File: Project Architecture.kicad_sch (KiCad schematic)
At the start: 0 parts

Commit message: Final Changes, Updated to Checked
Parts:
- added H1, H2, H3, H4: MountingHole_Pad, MountingHole:MountingHole_3.2mm_M3_DIN965_Pad, symbol Mechanical:MountingHole_Pad
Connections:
- no-connect marks 0 -> 4
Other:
- added sheet Section D - RTC (rtc.kicad_sch)
- sheet Section A - Title A ports: added I2C_SCL, I2C_SDA; removed none
- note added: "Page 9"

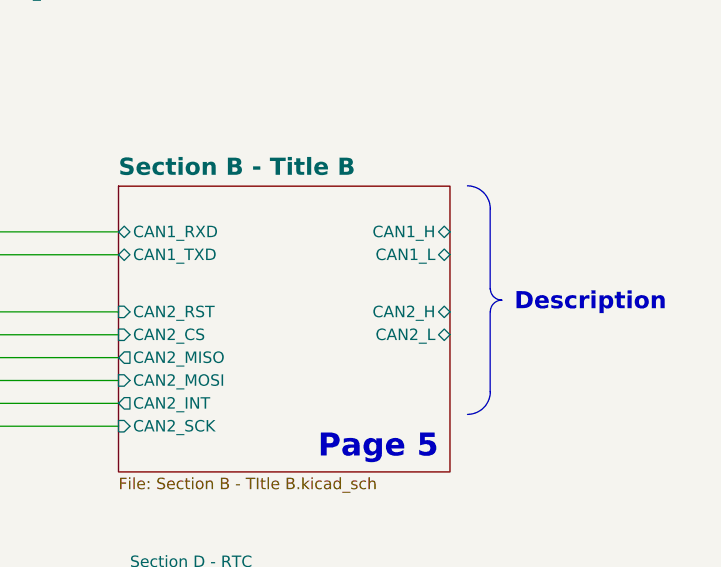
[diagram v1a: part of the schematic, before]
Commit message: Retry with rules DRC ERC passing
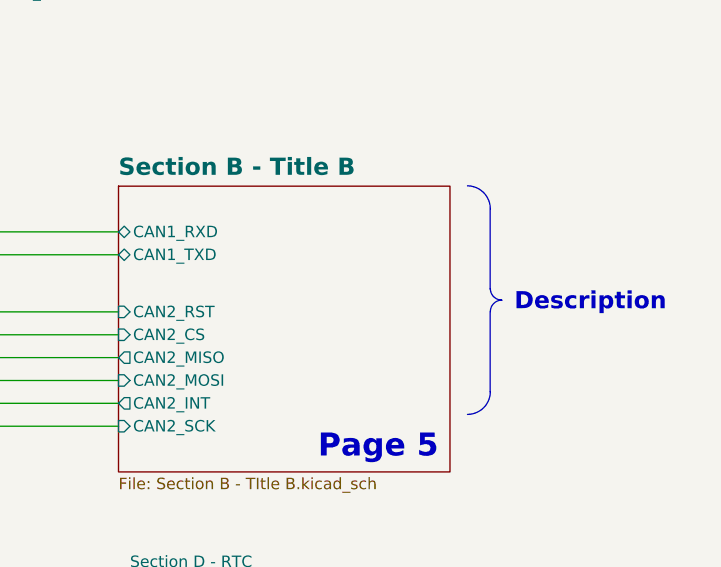
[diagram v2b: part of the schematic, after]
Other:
- sheet Section B - Title B ports: added none; removed CAN1_H, CAN1_L, CAN2_H, CAN2_L
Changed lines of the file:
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@@
-			)
-		)
-		(pin "CAN1_H" bidirectional
-			(at 266.7 149.86 0)
-			(effects
-				(font
-					(size 1.27 1.27)
-				)
-				(justify right)
-			)
-		)
-		(pin "CAN1_L" bidirectional
-			(at 266.7 152.4 0)
-			(effects
-				(font
-					(size 1.27 1.27)
-				)
-				(justify right)
 			)
 		)
@@
 			)
 		)
-		(pin "CAN2_H" bidirectional
-			(at 266.7 158.75 0)
-			(effects
-				(font
-					(size 1.27 1.27)
-				)
-				(justify right)
-			)
-		)
 		(pin "CAN2_INT" output
 			(at 229.87 168.91 180)
@@
 			)
 		)
-		(pin "CAN2_L" bidirectional
-			(at 266.7 161.29 0)
-			(effects
-				(font
-					(size 1.27 1.27)
-				)
-				(justify right)
-			)
-		)
